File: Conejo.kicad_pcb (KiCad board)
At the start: 4 copper layers, 130.3 x 112.5 mm, 104 parts, among them J1 BATT, J2 HRO_TYPE-C-31-M-12, J3 JTAG_TC2030, J4 RGB, Q1 2N7002, Q2 2N7002, Q3 AO3407, SW1 POWER, SW10 MX Hotswap, SW11 MX Hotswap, SW12 MX Hotswap, SW13 MX Hotswap, SW14 MX Hotswap, SW15 MX Hotswap, SW16 MX Hotswap, SW17 MX Hotswap, SW18 MX Hotswap, SW19 MX Hotswap, SW2 MX Hotswap, SW20 MX Hotswap, SW21 MX Hotswap, SW22 MX Hotswap, SW23 MX Hotswap, SW24 MX Hotswap, SW25 MX Hotswap, SW26 MX Hotswap, SW27 MX Hotswap, SW28 MX Hotswap, SW29 RESET, SW3 MX Hotswap, SW4 MX Hotswap, SW5 MX Hotswap, SW6 MX Hotswap, SW7 MX Hotswap, SW8 MX Hotswap, SW9 MX Hotswap, U1 BQ24075RGT, U2 MAX17048, U3 SRV05-4, U4 MS88SF3

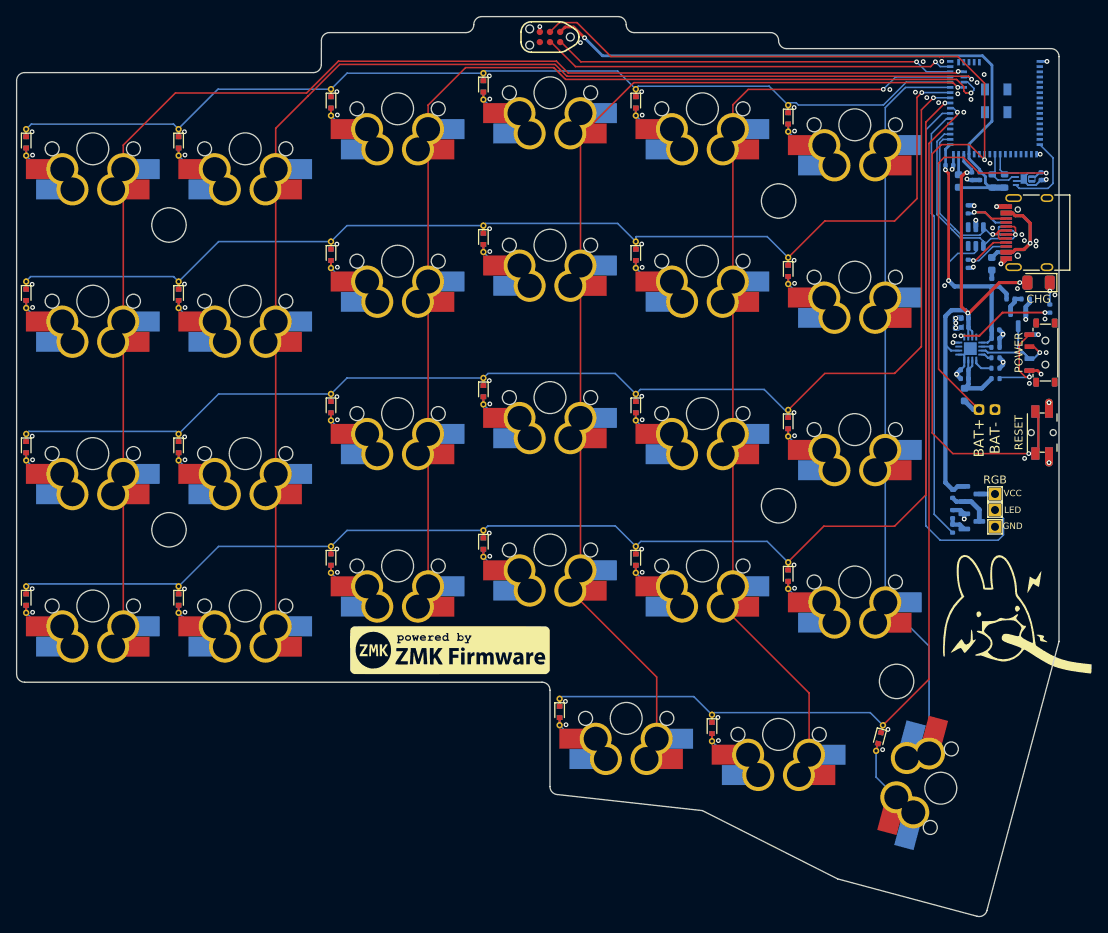
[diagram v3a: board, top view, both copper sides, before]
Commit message: feat(pcb): Version 0.3.2
- Move TC2030 footprint to accessible location
- Move diodes to be outside of 14mmx14mm switch area
- Update BOM to remove footprints that don't require placement
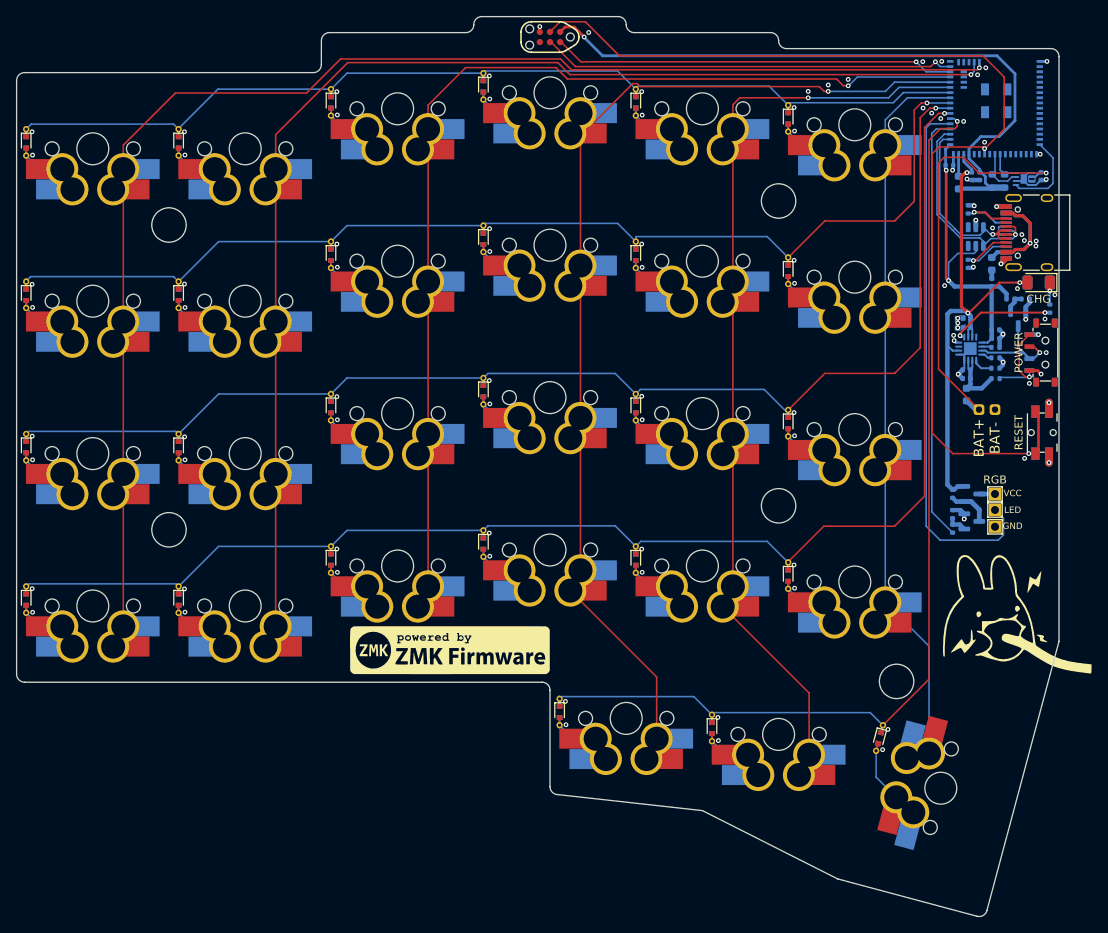
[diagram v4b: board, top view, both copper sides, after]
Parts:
- moved C3 0.25 mm to (109.2, 23.2)
- moved C4 0.25 mm to (109.2, 24.3)
- moved C6 0.25 mm to (109.2, 30.7)
- moved C7 0.25 mm to (109.2, 29.6)
- moved F1 0.25 mm to (109.2, 32.7)
- moved L1 0.20 mm to (108.2, 6.22)
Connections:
- U4 pad 38: unconnected-(U4-Pad38) -> EXT_PWR_EN
- U4 pad 39: unconnected-(U4-Pad39) -> LED_MOSI
- U4 pad 40: EXT_PWR_EN -> ROW5
- U4 pad 41: LED_MOSI -> ROW4
- U4 pad 42: ROW5 -> ROW3
- U4 pad 43: ROW4 -> ROW2
- U4 pad 44: ROW3 -> COL6
- U4 pad 45: ROW2 -> ROW1
- U4 pad 46: COL6 -> COL5
- U4 pad 47: ROW1 -> COL4
- U4 pad 48: COL5 -> COL3
- U4 pad 55: unconnected-(U4-Pad55) -> COL2
- U4 pad 56: unconnected-(U4-Pad56) -> COL1
- U4 pad 57: COL1 -> unconnected-(U4-Pad57)
- U4 pad 58: COL2 -> unconnected-(U4-Pad58)
- U4 pad 59: COL3 -> unconnected-(U4-Pad59)
- U4 pad 60: COL4 -> unconnected-(U4-Pad60)
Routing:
- net COL3: track 133.9 -> 128.8 mm
- net VDD: track 79.6 -> 84.5 mm
- net COL1: track 170.2 -> 173.0 mm
- net RESET: track 134.7 -> 136.5 mm
- net COL6: track 92.2 -> 90.7 mm
- net ROW2: track 137.6 -> 136.3 mm
- net COL4: track 130.1 -> 129.0 mm
- net ROW3: track 154.9 -> 153.9 mm
- net ROW4: track 172.4 -> 171.5 mm
- net ROW1: track 122.5 -> 121.7 mm
- net EXT_PWR_EN: track 54.1 -> 53.5 mm
- net COL5: track 111.8 -> 111.2 mm

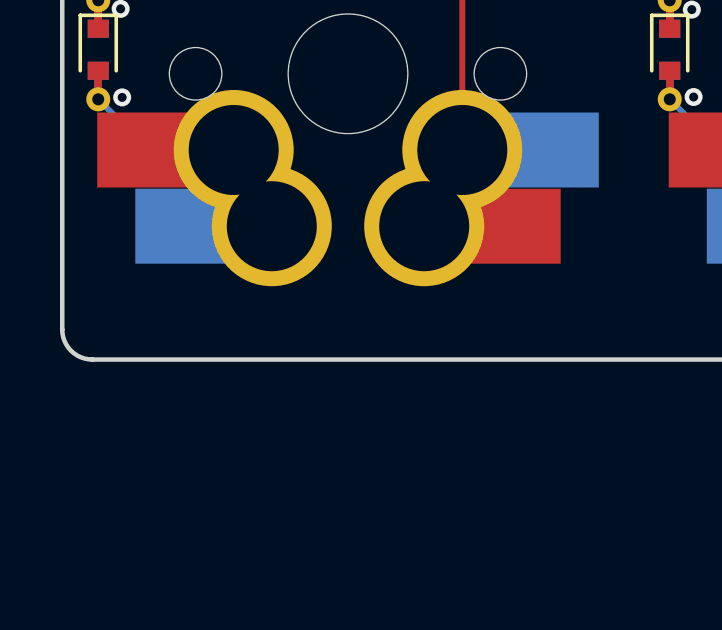
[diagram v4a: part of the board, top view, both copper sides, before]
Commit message: fix(pcb): Update Gerbers with JLCPCB order number location
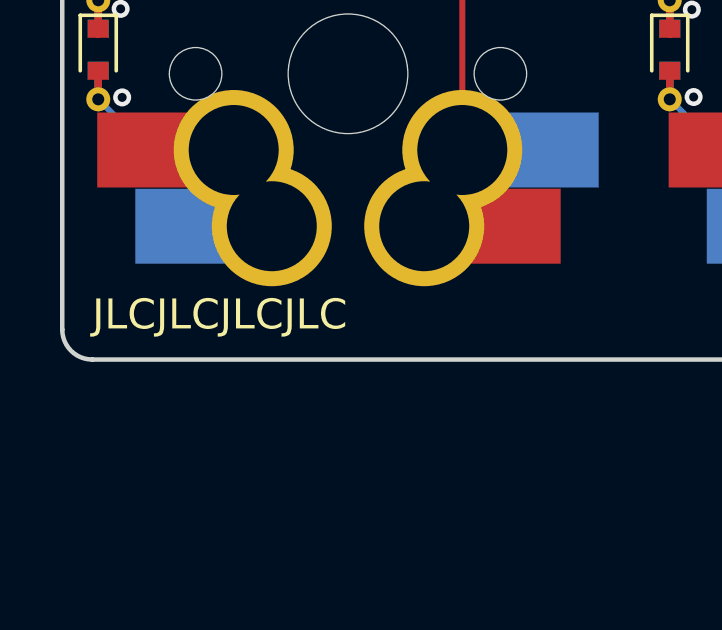
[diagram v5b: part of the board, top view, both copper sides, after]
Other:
- board text added: "JLCJLCJLCJLC"
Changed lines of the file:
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@@
     (effects (font (size 1 1) (thickness 0.2)))
+  )
+  (gr_text "JLCJLCJLCJLC" (at -8.525 67.175) (layer "F.SilkS")
+    (effects (font (size 1 1) (thickness 0.2)) (justify left))
   )
   (gr_text "Pinky2	-> 	Pinky:	0mm\nPinky 	-> 	Ring:	5mm\nRing 	-> 	Middle:	2mm\nMiddle 	-> 	Index:	2mm\nIndex 	-> 	Index2:	2mm\n" (at -13.675 100.025) (layer "Cmts.User")
